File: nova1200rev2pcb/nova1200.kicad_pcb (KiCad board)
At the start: 2 copper layers, 400.1 x 101.6 mm, 190 parts, among them J1 Conn_02x26_Odd_Even, J2 Conn_02x05_Top_Bottom, J3 Conn_02x05_Top_Bottom, J4 Conn_02x01, J5 Conn_02x09_Odd_Even, J6 Conn_01x09, SW1 SW_SPST, SW10 SW_SPST, SW11 SW_SPST, SW12 SW_SPST, SW13 SW_SPST, SW14 SW_SPST, SW15 SW_SPST, SW16 SW_SPST, SW17 SW_SPDT_MSM, SW18 SW_SPDT_MSM, SW19 SW_SPDT_MSM, SW2 SW_SPST, SW20 SW_SPDT_MSM, SW21 SW_SPDT_MSM, SW22 SW_SPDT_MSM, SW23 SW_SPDT_MSM, SW24 SW_SPDT_MSM, SW25 SW_SPDT_MSM, SW26 SW_SPDT_MSM, SW3 SW_SPST, SW4 SW_SPST, SW5 SW_SPST, SW6 SW_SPST, SW7 SW_SPST, SW8 SW_SPST, SW9 SW_SPST, U1 74LS257, U10 74LS173, U11 74LS173, U12 74LS173, U13 74LS173, U14 74LS173, U15 74LS257, U16 74LS42, U17 74LS42, U18 74LS02, U19 74LS06, U2 74LS257, U20 74LS06, U21 74LS06, U3 74LS257, U4 74LS257, U5 74LS173, U6 74LS173, U7 74LS173, U8 74LS173, U9 74LS173

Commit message: Fixed error in pcb where EXEC and DEFER where swapped
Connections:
- J1 pad 50: /DEFER -> /EXEC
- J1 pad 52: /EXEC -> /DEFER
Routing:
- net /DEFER: track 404.9 -> 410.5 mm
- net /EXEC: track 427.8 -> 429.0 mm, vias 2 -> 3
- net /ND0: track 244.8 -> 245.5 mm
- net /ND11: track 446.4 -> 445.8 mm
- net /PL: track 97.9 -> 97.3 mm

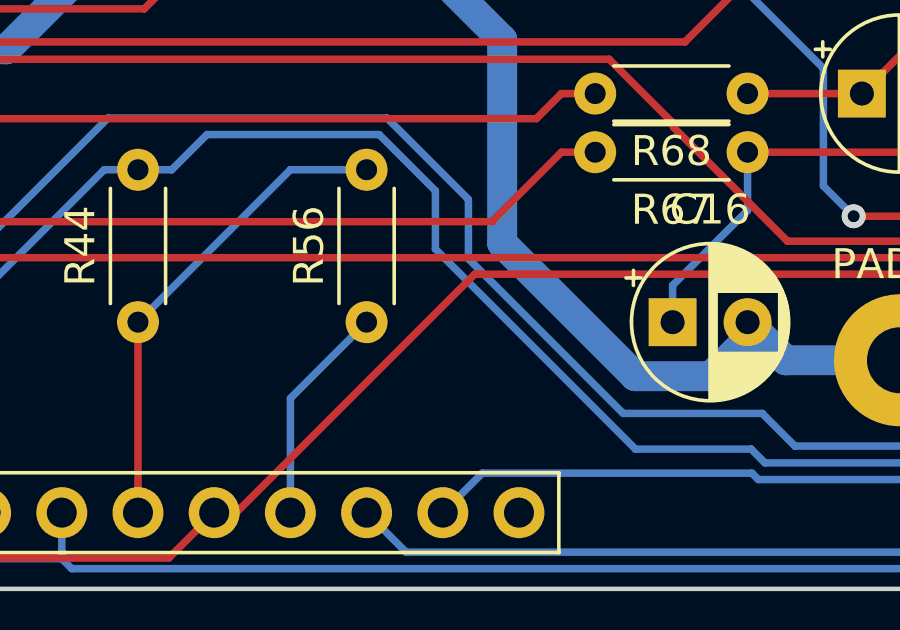
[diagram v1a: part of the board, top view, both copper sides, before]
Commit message: Added jumper/resistor for Teensy application
// Nano to Teensy mapping:
//Arduino Teensy 3.5 Application
//GND	GND	GND
//D2	D0	D0
//..	..	..
//D12	D10	ENLCD1
//D13	A1	ENLCD2
//A0	A4	--- (KEYP)
//A1	A5	---
//A2	A6	LCD4
//A3	A7	LCD5
//A4	A8	LCD6
//A5	A9	LCD7
//A6	X (3.3 V)	---
//A7	--- (AGND)	---
//5V	Vin	5V
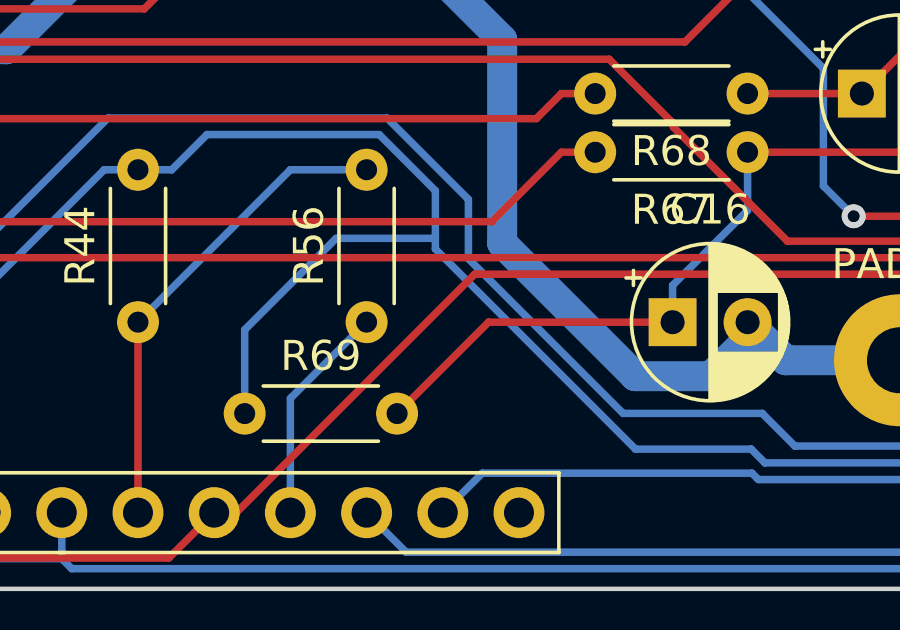
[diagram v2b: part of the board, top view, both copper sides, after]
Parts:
- added R69: Jumper, Resistor_THT:R_Axial_DIN0204_L3.6mm_D1.6mm_P5.08mm_Horizontal, F.Cu at (346.5, 111.0)
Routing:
- net /KEYL: track 52.8 -> 63.3 mm
- net /KEYP: track 137.4 -> 147.9 mm
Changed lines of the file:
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@@
     (thickness 1.6)
     (drawings 64)
-    (tracks 3687)
+    (tracks 3693)
     (zones 0)
-    (modules 190)
+    (modules 191)
     (nets 189)
   )
@@
     (add_net /VCC)
   )
+  (module Resistor_THT:R_Axial_DIN0204_L3.6mm_D1.6mm_P5.08mm_Horizontal (layer F.Cu)
+    (at 346.456 110.998)
+    (descr "Resistor, Axial_DIN0204 series, Axial, Horizontal, pin pitch=5.08mm, 0.167W, length*diameter=3.6*1.6mm^2, http://cdn-reichelt.de/documents/datenblatt/B400/1_4W%23YAG.pdf")
+    (tags "Resistor Axial_DIN0204 series Axial Horizontal pin pitch 5.08mm 0.167W length 3.6mm diameter 1.6mm")
+    (fp_text reference R69 (at 2.54 -1.92) (layer F.SilkS)
+      (effects (font (size 1 1) (thickness 0.15)))
+    )
+    (fp_text value Jumper (at 2.54 1.92) (layer F.Fab)
+      (effects (font (size 1 1) (thickness 0.15)))
+    )
+    (fp_line (start 0.74 -0.8) (end 0.74 0.8) (layer F.Fab) (width 0.1))
+    (fp_line (start 0.74 0.8) (end 4.34 0.8) (layer F.Fab) (width 0.1))
+    (fp_line (start 4.34 0.8) (end 4.34 -0.8) (layer F.Fab) (width 0.1))
+    (fp_line (start 4.34 -0.8) (end 0.74 -0.8) (layer F.Fab) (width 0.1))
+    (fp_line (start 0 0) (end 0.74 0) (layer F.Fab) (width 0.1))
+    (fp_line (start 5.08 0) (end 4.34 0) (layer F.Fab) (width 0.1))
+    (fp_line (start 0.62 -0.92) (end 4.46 -0.92) (layer F.SilkS) (width 0.12))
+    (fp_line (start 0.62 0.92) (end 4.46 0.92) (layer F.SilkS) (width 0.12))
+    (fp_line (start -0.95 -1.05) (end -0.95 1.05) (layer F.CrtYd) (width 0.05))
+    (fp_line (start -0.95 1.05) (end 6.03 1.05) (layer F.CrtYd) (width 0.05))
+    (fp_line (start 6.03 1.05) (end 6.03 -1.05) (layer F.CrtYd) (width 0.05))
+    (fp_line (start 6.03 -1.05) (end -0.95 -1.05) (layer F.CrtYd) (width 0.05))
+    (fp_text user %R (at 2.54 0) (layer F.Fab)
+      (effects (font (size 0.72 0.72) (thickness 0.108)))
+    )
+    (pad 1 thru_hole circle (at 0 0) (size 1.4 1.4) (drill 0.7) (layers *.Cu *.Mask)
+      (net 126 /KEYP))
+    (pad 2 thru_hole oval (at 5.08 0) (size 1.4 1.4) (drill 0.7) (layers *.Cu *.Mask)
+      (net 120 /KEYL))
+    (model ${KISYS3DMOD}/Resistor_THT.3dshapes/R_Axial_DIN0204_L3.6mm_D1.6mm_P5.08mm_Horizontal.wrl
+      (at (xyz 0 0 0))
+      (scale (xyz 1 1 1))
+      (rotate (xyz 0 0 0))
+    )
+  )
   (module MountingHole:MountingHole_3.2mm_M3_Pad (layer F.Cu)
     (at 237.49 97.8)
@@
   (segment (start 363.22 25.4) (end 363.22 26.6253) (width 0.25) (layer F.Cu) (net 70))
   (via (at 130.9331 51.0772) (size 0.8) (layers F.Cu B.Cu) (net 70))
-  (segment (start 358.1428 42.4604) (end 350.7607 42.4604) (width 0.25) (layer F.Cu) (net 71))
-  (segment (start 350.7607 42.4604) (end 347.7118 45.5093) (width 0.25) (layer F.Cu) (net 71))
-  (segment (start 347.7118 45.5093) (end 254.9567 45.5093) (width 0.25) (layer F.Cu) (net 71))
-  (segment (start 254.9567 45.5093) (end 254.6239 45.8421) (width 0.25) (layer F.Cu) (net 71))
-  (segment (start 254.6239 45.8421) (end 253.8457 45.8421) (width 0.25) (layer F.Cu) (net 71))
-  (segment (start 253.8457 45.8421) (end 253.2954 46.3924) (width 0.25) (layer F.Cu) (net 71))
-  (segment (start 253.2954 46.3924) (end 234.8709 46.3924) (width 0.25) (layer F.Cu) (net 71))
-  (segment (start 234.8709 46.3924) (end 232.4454 48.8179) (width 0.25) (layer F.Cu) (net 71))
-  (segment (start 232.4454 48.8179) (end 167.0026 48.8179) (width 0.25) (layer F.Cu) (net 71))
-  (segment (start 167.0026 48.8179) (end 166.1209 49.6996) (width 0.25) (layer F.Cu) (net 71))
-  (segment (start 166.1209 49.6996) (end 106.3227 49.6996) (width 0.25) (layer F.Cu) (net 71))
-  (segment (start 106.3227 49.6996) (end 105.9641 49.341) (width 0.25) (layer F.Cu) (net 71))
-  (segment (start 105.9641 49.341) (end 96.6865 49.341) (width 0.25) (layer F.Cu) (net 71))
-  (segment (start 96.6865 49.341) (end 96.1356 49.8919) (width 0.25) (layer F.Cu) (net 71))
-  (segment (start 96.1356 49.8919) (end 95.4519 49.8919) (width 0.25) (layer F.Cu) (net 71))
-  (segment (start 95.4519 49.8919) (end 95.0815 49.5215) (width 0.25) (layer F.Cu) (net 71))
-  (segment (start 95.0815 49.5215) (end 84.1052 49.5215) (width 0.25) (layer F.Cu) (net 71))
-  (segment (start 84.1052 49.5215) (end 83.8469 49.7798) (width 0.25) (layer F.Cu) (net 71))
   (segment (start 31.67 102.87) (end 32.4994 102.87) (width 0.25) (layer B.Cu) (net 70))
   (segment (start 58.470463 103.275032) (end 61.415494 100.33) (width 0.25) (layer F.Cu) (net 70))
@@
   (segment (start 98.044 100.668152) (end 99.101157 101.725309) (width 0.25) (layer B.Cu) (net 70))
   (segment (start 98.044 100.33) (end 98.044 100.668152) (width 0.25) (layer B.Cu) (net 70))
+  (segment (start 358.1428 42.4604) (end 350.7607 42.4604) (width 0.25) (layer F.Cu) (net 71))
+  (segment (start 350.7607 42.4604) (end 347.7118 45.5093) (width 0.25) (layer F.Cu) (net 71))
+  (segment (start 347.7118 45.5093) (end 254.9567 45.5093) (width 0.25) (layer F.Cu) (net 71))
+  (segment (start 254.9567 45.5093) (end 254.6239 45.8421) (width 0.25) (layer F.Cu) (net 71))
+  (segment (start 254.6239 45.8421) (end 253.8457 45.8421) (width 0.25) (layer F.Cu) (net 71))
+  (segment (start 253.8457 45.8421) (end 253.2954 46.3924) (width 0.25) (layer F.Cu) (net 71))
+  (segment (start 253.2954 46.3924) (end 234.8709 46.3924) (width 0.25) (layer F.Cu) (net 71))
+  (segment (start 234.8709 46.3924) (end 232.4454 48.8179) (width 0.25) (layer F.Cu) (net 71))
+  (segment (start 232.4454 48.8179) (end 167.0026 48.8179) (width 0.25) (layer F.Cu) (net 71))
+  (segment (start 167.0026 48.8179) (end 166.1209 49.6996) (width 0.25) (layer F.Cu) (net 71))
+  (segment (start 166.1209 49.6996) (end 106.3227 49.6996) (width 0.25) (layer F.Cu) (net 71))
+  (segment (start 106.3227 49.6996) (end 105.9641 49.341) (width 0.25) (layer F.Cu) (net 71))
+  (segment (start 105.9641 49.341) (end 96.6865 49.341) (width 0.25) (layer F.Cu) (net 71))
+  (segment (start 96.6865 49.341) (end 96.1356 49.8919) (width 0.25) (layer F.Cu) (net 71))
+  (segment (start 96.1356 49.8919) (end 95.4519 49.8919) (width 0.25) (layer F.Cu) (net 71))
+  (segment (start 95.4519 49.8919) (end 95.0815 49.5215) (width 0.25) (layer F.Cu) (net 71))
+  (segment (start 95.0815 49.5215) (end 84.1052 49.5215) (width 0.25) (layer F.Cu) (net 71))
+  (segment (start 84.1052 49.5215) (end 83.8469 49.7798) (width 0.25) (layer F.Cu) (net 71))
   (segment (start 44.8842 90.4852) (end 44.8842 67.2828) (width 0.25) (layer B.Cu) (net 71))
   (segment (start 44.8842 67.2828) (end 48.4927 63.6743) (width 0.25) (layer B.Cu) (net 71))
@@
   (segment (start 363.22 104.2247) (end 360.72 106.7247) (width 0.25) (layer B.Cu) (net 120))
   (segment (start 405.13 92.71) (end 403.9047 92.71) (width 0.25) (layer F.Cu) (net 120))
+  (segment (start 354.584 107.95) (end 351.536 110.998) (width 0.25) (layer F.Cu) (net 120))
+  (segment (start 360.72 107.95) (end 354.584 107.95) (width 0.25) (layer F.Cu) (net 120))
   (segment (start 367.03 100.33) (end 363.22 100.33) (width 0.25) (layer F.Cu) (net 121))
   (segment (start 401.3647 92.71) (end 401.3647 93.1695) (width 0.25) (layer F.Cu) (net 121))
@@
   (segment (start 363.3418 112.182) (end 359.4827 112.182) (width 0.25) (layer B.Cu) (net 126))
   (segment (start 359.4827 112.182) (end 352.8131 105.5124) (width 0.25) (layer B.Cu) (net 126))
-  (segment (start 352.8131 105.5124) (end 352.8131 103.5696) (width 0.25) (layer B.Cu) (net 126))
   (segment (start 352.8131 103.5696) (end 350.9396 101.6961) (width 0.25) (layer B.Cu) (net 126))
   (segment (start 350.9396 101.6961) (end 345.1992 101.6961) (width 0.25) (layer B.Cu) (net 126))
@@
   (segment (start 342.9 102.87) (end 341.7747 102.87) (width 0.25) (layer B.Cu) (net 126))
   (via (at 400.0887 63.6338) (size 0.8) (layers F.Cu B.Cu) (net 126))
+  (segment (start 346.456 110.998) (end 346.456 108.204) (width 0.25) (layer B.Cu) (net 126))
+  (segment (start 346.456 108.204) (end 349.504 105.156) (width 0.25) (layer B.Cu) (net 126))
+  (segment (start 349.504 105.156) (end 352.8131 105.156) (width 0.25) (layer B.Cu) (net 126))
+  (segment (start 352.8131 105.5124) (end 352.8131 105.156) (width 0.25) (layer B.Cu) (net 126))
+  (segment (start 352.8131 105.156) (end 352.8131 103.5696) (width 0.25) (layer B.Cu) (net 126))
   (segment (start 384.81 92.71) (end 384.81 91.4847) (width 0.25) (layer B.Cu) (net 128))
   (segment (start 384.81 83.82) (end 384.81 85.0953) (width 0.25) (layer B.Cu) (net 128))
